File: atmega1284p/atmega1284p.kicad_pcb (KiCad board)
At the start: 2 copper layers, 48.3 x 99.1 mm, 38 parts, among them J1 PA, J10 AVR-ISP-6, J11 USB_B_Mini, J12 CC1101_Breakout, J2 PB, J3 PC, J4 PD, J5 I2C1, J6 I2C2, J7 Power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

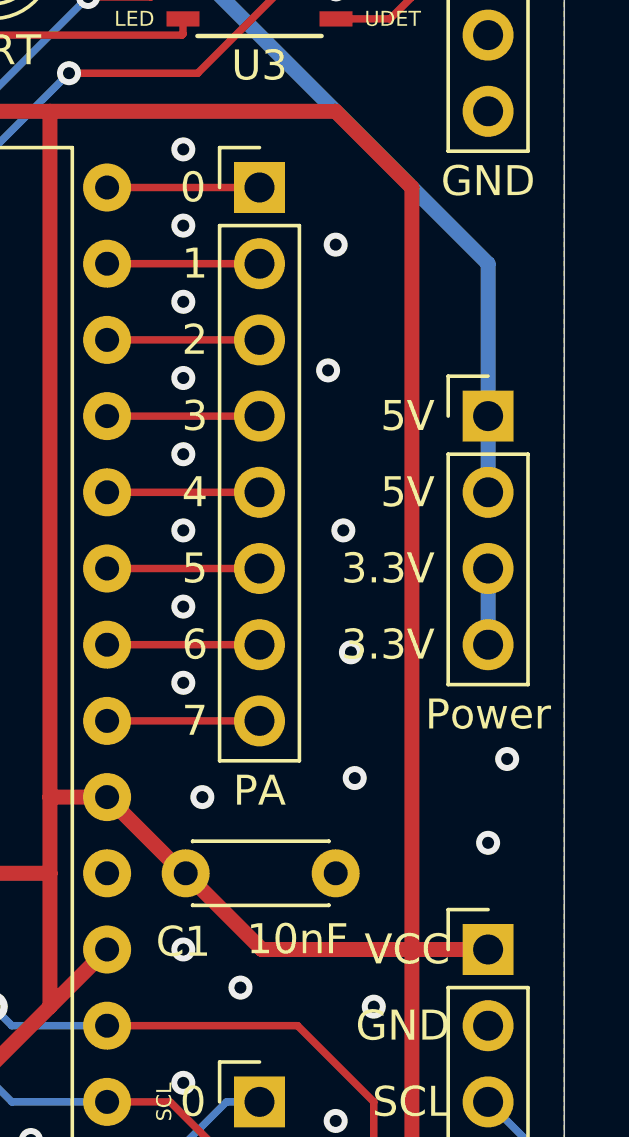
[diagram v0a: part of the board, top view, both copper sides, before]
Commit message: Fixed net of 3.3V pins
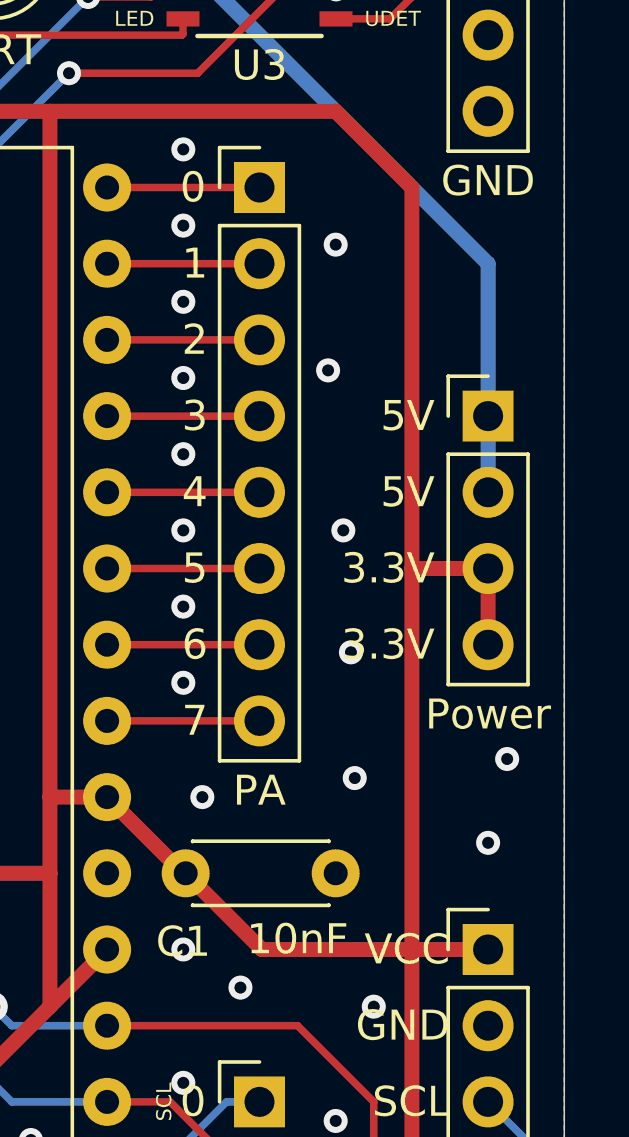
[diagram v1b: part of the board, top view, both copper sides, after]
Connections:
- J7 pad 3: +3V3 -> VCC
- J7 pad 4: +3V3 -> VCC
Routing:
- net VCC: track 262.5 -> 267.6 mm
- net +3V3: track 2.54 -> 0.00 mm

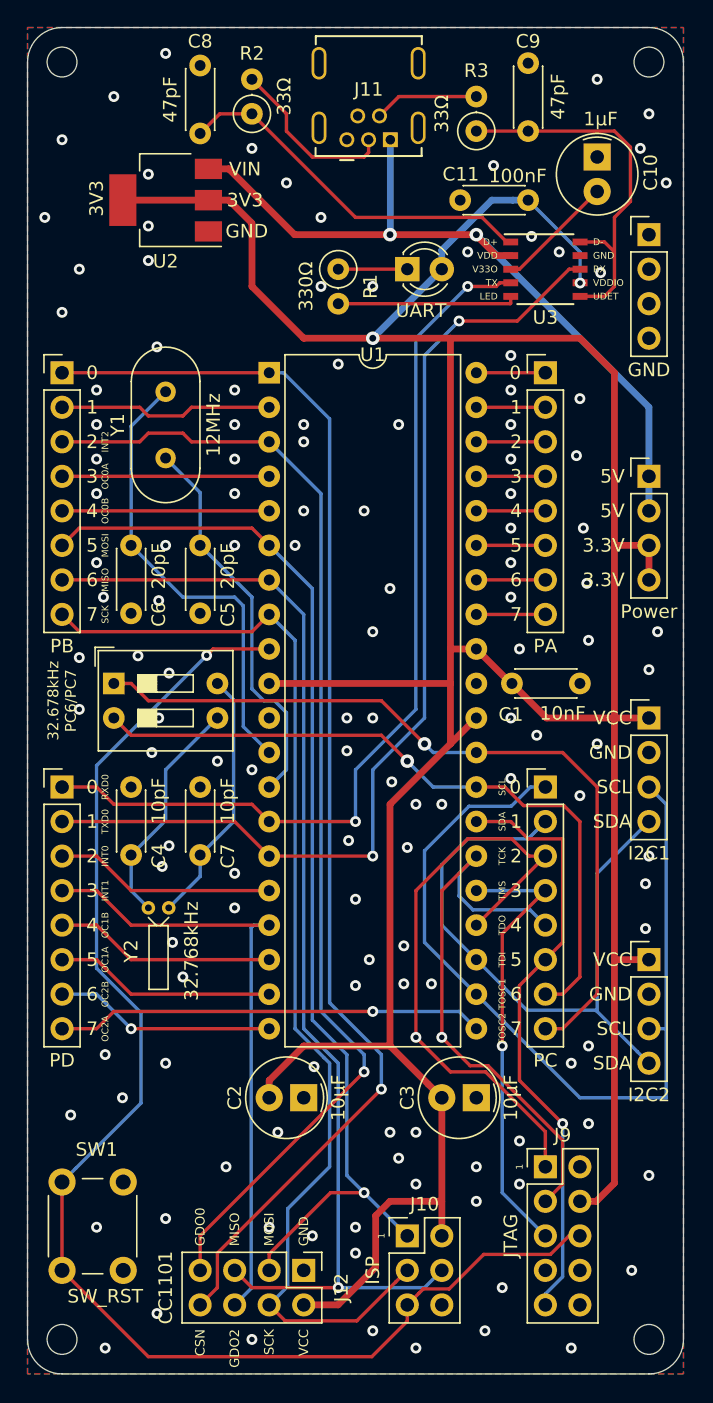
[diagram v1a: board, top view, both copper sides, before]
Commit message: treewide: Update to KiCAD 7
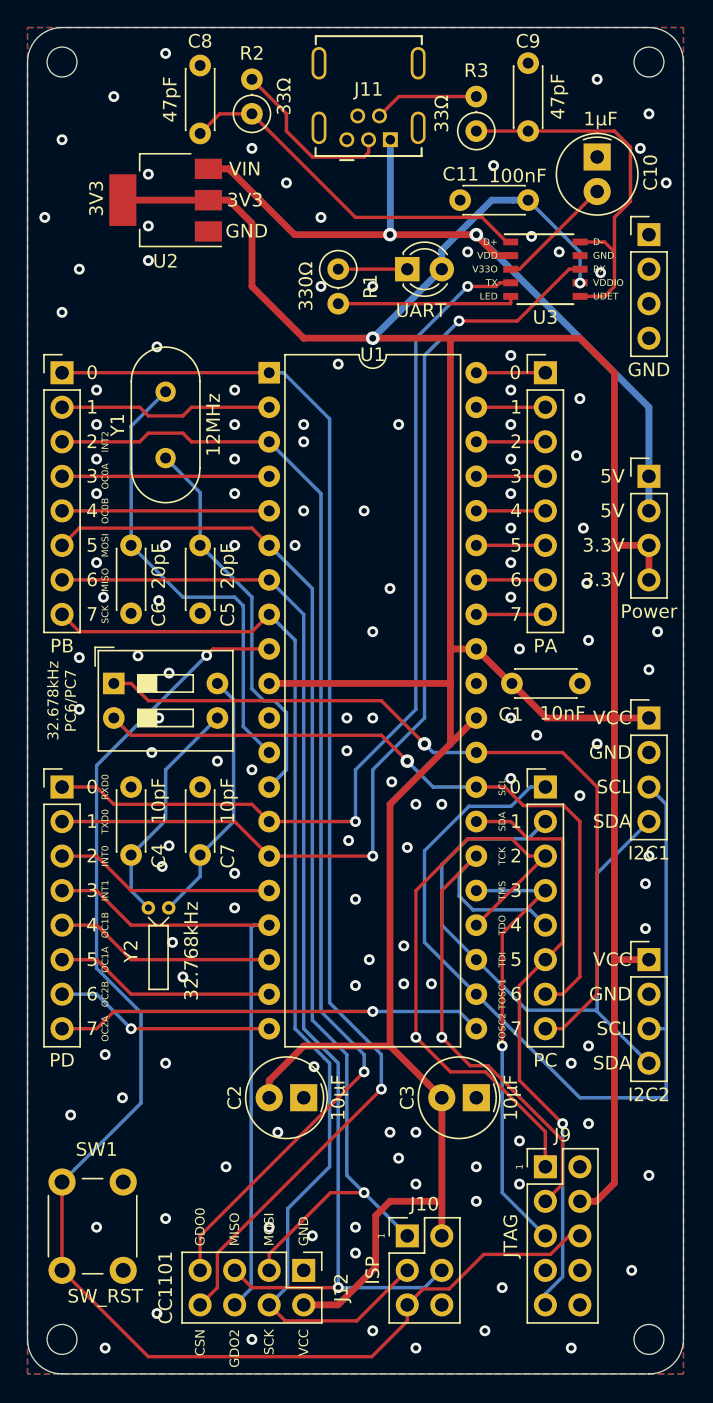
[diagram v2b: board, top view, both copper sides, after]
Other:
- net class Default removed
- net class Power removed

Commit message: atmega1284p: Use CH340N as TTL adapter
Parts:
- removed C10: 1µF, boards:electrolytic_capacitor_10uf
- removed C11: 100nF, Capacitor_THT:C_Disc_D4.3mm_W1.9mm_P5.00mm
- removed D1: LED, LED_THT:LED_D3.0mm
- removed R1: 330Ω, Resistor_THT:R_Axial_DIN0207_L6.3mm_D2.5mm_P2.54mm_Vertical
- removed R2, R3: 33Ω, Resistor_THT:R_Axial_DIN0207_L6.3mm_D2.5mm_P2.54mm_Vertical
- C8, C9: value 47pF -> 100nF
- U3: value HT42B534-1 -> CH340N; footprint boards:HT42B534-1SOP10 -> Package_SO:SOP-8_3.9x4.9mm_P1.27mm
- moved C8 21.9 mm to (138.5, 59.0), turned to 0 degrees
- moved C9 8.03 mm to (143.5, 68.6), turned to 180 degrees
- moved U3 7.61 mm to (140.9, 63.6)
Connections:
- C8 pad 2: Net-(C8-Pad2) -> VCC
- C9 pad 1: Net-(C9-Pad1) -> VCC
- J11 pad 2: Net-(J11-Pad2) -> Net-(J11-D-)
- J11 pad 3: Net-(J11-Pad3) -> Net-(J11-D+)
- J11 pad 4: Net-(J11-Pad4) -> unconnected-(J11-ID-Pad4)
- J9 pad 7: Net-(J9-Pad7) -> unconnected-(J9-VCC-Pad7)
- J9 pad 8: Net-(J9-Pad8) -> unconnected-(J9-~{TRST}-Pad8)
- U3 pad 1: Net-(C8-Pad2) -> Net-(J11-D+)
- U3 pad 2: +5V -> Net-(J11-D-)
- U3 pad 3: Net-(C10-Pad1) -> GND
- U3 pad 4: /PD0_RXD0 -> unconnected-(U3-~{RTS}-Pad4)
- U3 pad 5: Net-(R1-Pad2) -> VCC
- U3 pad 6: Net-(C9-Pad1) -> /PD0_RXD0
- U3 pad 7: VCC -> /PD1_TXD0
- U3 pad 8: /PD1_TXD0 -> VCC
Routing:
- net Net-(C9-Pad1): track 28.2 -> 0.00 mm
- net Net-(C8-Pad2): track 27.4 -> 0.00 mm
- net Net-(J11-D-): track 0.00 -> 15.2 mm
- net Net-(R1-Pad2): track 13.2 -> 0.00 mm
- net Net-(J11-Pad3): track 12.8 -> 0.00 mm
- net /PD0_RXD0: track 68.7 -> 79.9 mm
- net Net-(J11-D+): track 0.00 -> 11.1 mm
- net VCC: track 267.6 -> 256.8 mm, vias 2 -> 0
- net Net-(C10-Pad1): track 8.73 -> 0.00 mm
- net Net-(J11-Pad2): track 7.72 -> 0.00 mm
- net Net-(D1-Pad1): track 5.08 -> 0.00 mm
- net /PD1_TXD0: track 76.4 -> 81.4 mm
- net +5V: track 57.5 -> 53.5 mm, vias 2 -> 1
- net GND: vias 132 -> 136
- net /PC4_TDO: vias 1 -> 0
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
